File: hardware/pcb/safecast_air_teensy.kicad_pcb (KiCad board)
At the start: 2 copper layers, 108 x 69.8 mm, 49 parts, among them P1 CONN_5X2, P10 CONN_5_MOD, P2 CONN_5X2, P3 CONN_5X2, P4 CONN_2X2, P5 CONN_2, P6 CONN_2, P7 CONN_2, P8 CONN_2, P9 CONN_2, U1 GPS, U2 XBEE, U3 LCD, U4 OPENLOG, U5 POLOLU_3V3, U6 TEENSY3.1, U7 R5_BUSSED

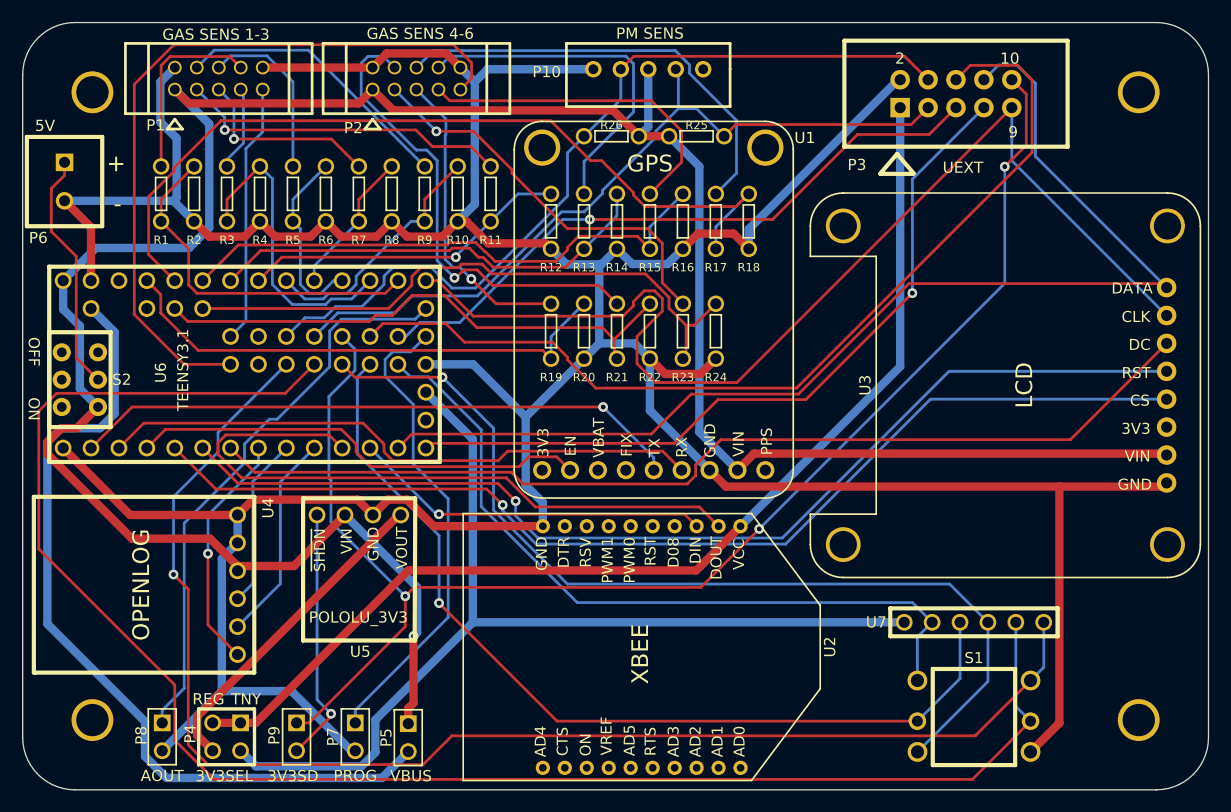
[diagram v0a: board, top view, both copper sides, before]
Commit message: Added header for opc-n2 particle counter. Changed pin used for pwm2 as d33 pin can't be low during reboot of teensy. Swapped with UEXT_CS.  Removed optional shutdown for external 3v3 regulator - as pin used for this was dual use with UEXT chip select. Used extra free pins (after joyswitch modifications) for the UEXT RX and TX pins.
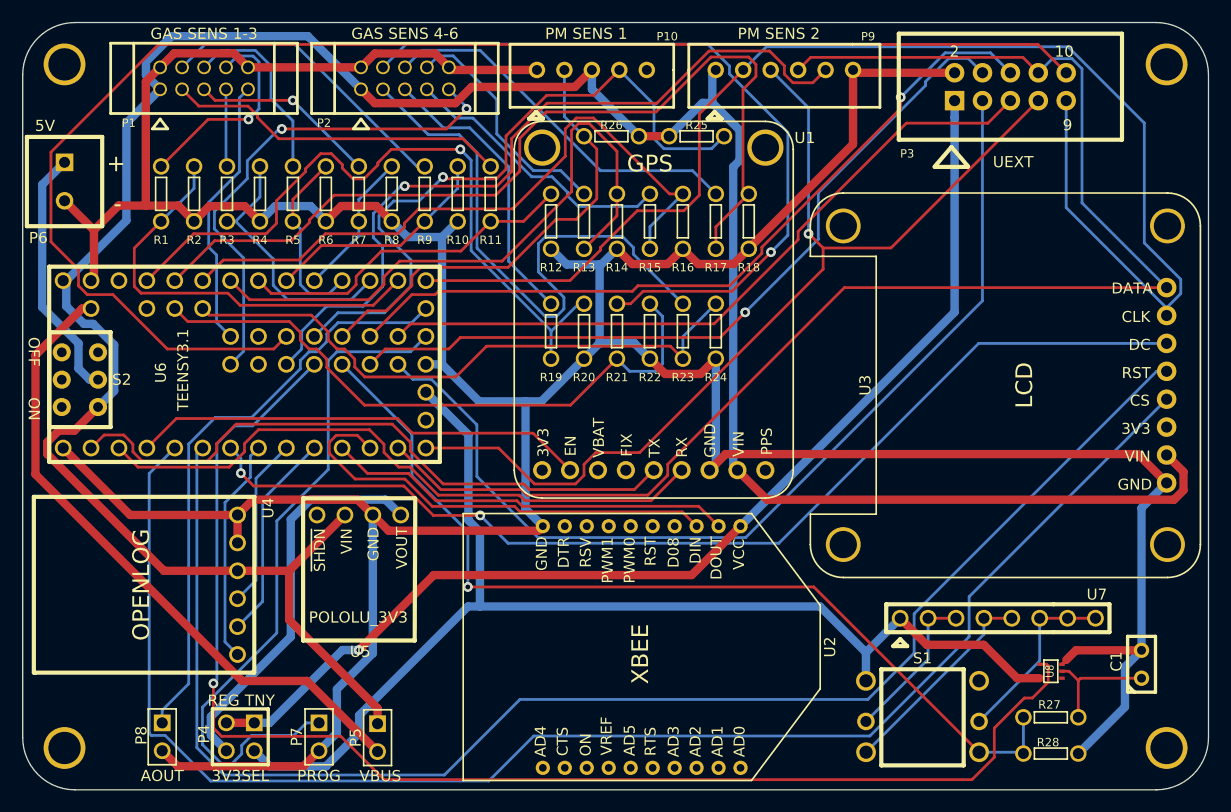
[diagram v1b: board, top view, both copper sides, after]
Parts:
- added C1: 0.1uf, C1, F.Cu at (127.3, 83.8)
- added R27: 20k, R_SMALL, F.Cu at (119.0, 88.6)
- added R28: 12k, R_SMALL, F.Cu at (119.0, 91.9)
- added U8: SCHMITT, SOT353, F.Cu at (119.0, 84.5)
- P9: value CONN_2 -> CONN_6; footprint PIN_ARRAY_2X1 -> JST_XH_6PIN
- U7: value R5_BUSSED -> R4_ISOLATED; footprint R5_BUSSED -> R8_ISOLATED
- moved P9 75.2 mm to (94.7, 29.7), turned to 0 degrees
- moved P10 5.13 mm to (77.2, 29.7)
- moved P3 4.99 mm to (115.3, 31.2)
- moved S1 4.69 mm to (107.3, 89.0)
- moved H1 3.59 mm to (29.2, 29.2)
- moved H2 3.59 mm to (129.5, 29.2)
- moved H4 3.59 mm to (29.2, 91.4)
- moved H3 3.59 mm to (129.5, 91.4)
- moved P7 3.30 mm to (52.4, 90.4)
- moved P5 2.79 mm to (57.7, 90.5)
- moved U7 2.20 mm to (114.2, 79.6)
- moved P1 1.34 mm to (41.9, 30.5)
- moved P4 1.25 mm to (45.2, 90.4)
- moved P2 1.05 mm to (60.2, 30.5)
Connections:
- P3 pad 10: /D31 -> /UEXT_CS
- P3 pad 3: /PWM1 -> /UEXT_TX
- P3 pad 4: /PWM2 -> /UEXT_RX
- P9 pad 1: /D31 -> /5V
- P9 pad 2: /3V3_REG_SHDN -> /SCK
- S1 pad 1: /JOY_A -> /3V3_TNSY
- S1 pad 4: GND -> /JOY_COMM
- U5 pad 1: /3V3_REG_SHDN -> (no net)
- U6 pad 36: /JOY_CENT -> /PM_CS
- U6 pad 37: /JOY_D -> N-0000012
- U6 pad 38: /JOY_C -> /JOY_COMM
- U6 pad 39: /JOY_B -> /UEXT_RX
- U6 pad 40: /JOY_A -> /UEXT_TX
- U6 pad 43: /D31 -> /PWM2
- U6 pad 45: /PWM2 -> /UEXT_CS
- U7 pad 2: /JOY_A -> /JOY_B
- U7 pad 5: /JOY_D -> /JOY_C
- U7 pad 6: /JOY_CENT -> /JOY_D
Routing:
- net /JOY_D: track 153.1 -> 16.8 mm
- net /UEXT_CS: track 0.00 -> 132.5 mm
- net /D31: track 130.6 -> 0.00 mm, vias 3 -> 0
- net /JOY_CENT: track 125.8 -> 0.00 mm, vias 1 -> 0
- net N-0000012: track 0.00 -> 123.4 mm, vias 0 -> 1
- net /UEXT_TX: track 0.00 -> 89.6 mm
- net /JOY_COMM: track 0.00 -> 85.1 mm, vias 0 -> 1
- net /PM_CS: track 0.00 -> 70.8 mm, vias 0 -> 1
- net /UEXT_RX: track 0.00 -> 70.5 mm, vias 0 -> 1
- net /JOY_B: track 83.9 -> 14.3 mm, vias 1 -> 0
- net /JOY_A: track 68.3 -> 0.00 mm
- net /JOY_C: track 87.3 -> 19.2 mm, vias 1 -> 0
- net /LCD_CS: track 99.7 -> 137.9 mm, vias 1 -> 0
- net /LCD_RST: track 98.2 -> 134.1 mm, vias 1 -> 0
- net /PWM2: track 75.8 -> 41.8 mm
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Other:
- board text added: "PM SENS 1"
- board text added: "PM SENS 2"
- board text removed: "3V3SD"
- board text removed: "PM SENS"
